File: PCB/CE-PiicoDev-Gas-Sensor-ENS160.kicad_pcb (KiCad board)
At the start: 2 copper layers, 25.4 x 25.4 mm, 34 parts, among them J1 , J2 , J3 Conn_01x05_Male, U1 ENS160, U2 Regulator 1V8

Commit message: v00
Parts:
- moved U2 4.13 mm to (93.6, 105.2), turned to 180 degrees
- moved R4 0.71 mm to (103.5, 106.6)
- moved C1 0.13 mm to (97.8, 98.8)
- renumbered ASW to ASW1
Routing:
- net +3V3: track 74.9 -> 79.8 mm
- net Net-(ASW1-Pad1): track 22.0 -> 24.4 mm, vias 0 -> 2
- net GND: track 10.2 -> 11.5 mm, vias 6 -> 8
- net /SCL: track 52.6 -> 53.8 mm

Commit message: Update CE-PiicoDev-Gas-Sensor-ENS160.kicad_pcb
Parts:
- removed kibuzzard-6271D9EE (x2): G***, kibuzzard-6271D9EE
- removed kibuzzard-6271DA35 (x2): G***, kibuzzard-6271DA35
- removed kibuzzard-6271DA5A (x2): G***, kibuzzard-6271DA5A
- removed kibuzzard-6271DA98 (x2): G***, kibuzzard-6271DA98
- removed kibuzzard-6271DAC1 (x2): G***, kibuzzard-6271DAC1
- added kibuzzard-62749DE2: G***, kibuzzard-62749DE2, B.Cu at (94.7, 110.1)
- added kibuzzard-62749DFD: G***, kibuzzard-62749DFD, F.Cu at (97.3, 110.0)
- added kibuzzard-62749DFD: G***, kibuzzard-62749DFD, B.Cu at (97.3, 110.0)
- added kibuzzard-62749E20: G***, kibuzzard-62749E20, F.Cu at (102.4, 110.4)
- added kibuzzard-62749E20: G***, kibuzzard-62749E20, B.Cu at (102.4, 110.4)
- added kibuzzard-62749E58: G***, kibuzzard-62749E58, F.Cu at (92.2, 110.1)
- added kibuzzard-62749E58: G***, kibuzzard-62749E58, B.Cu at (92.2, 110.1)
- added kibuzzard-62749E78: G***, kibuzzard-62749E78, F.Cu at (99.8, 109.9)
- added kibuzzard-62749E78: G***, kibuzzard-62749E78, B.Cu at (99.8, 109.9)
- added kibuzzard-62749F0B: G***, kibuzzard-62749F0B, F.Cu at (94.7, 110.1)
- renumbered ASW1 to ASW
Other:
- board text added: "ASW"
- board text added: "Designed at Core Electronics by Peter Johnston"
- board text added: "Pin Label Settings: font=Roboto-Bold text=GND l-cap=[ r-cap=] align=Right height=1.1 width=4.6 pad-top=3 pad-left=16 pad-right=3 pad-bot=3"
- board text removed: "Designed at Core Electronics"
- board text removed: "Pin Label Settings: font=Roboto text=GND l-cap=[ r-cap=] align=Left height=1.1 width=4.6 pad-top=2.5 pad-left=16 pad-right=2.5 pad-bot=2.5"

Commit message: Update CE-PiicoDev-Gas-Sensor-ENS160.kicad_pcb
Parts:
- removed kibuzzard-62749DE2: G***, kibuzzard-62749DE2
- removed kibuzzard-62749DFD (x2): G***, kibuzzard-62749DFD
- removed kibuzzard-62749E20 (x2): G***, kibuzzard-62749E20
- removed kibuzzard-62749E58 (x2): G***, kibuzzard-62749E58
- removed kibuzzard-62749E78 (x2): G***, kibuzzard-62749E78
- removed kibuzzard-62749F0B: G***, kibuzzard-62749F0B
- added kibuzzard-6285E559: G***, kibuzzard-6285E559, F.Cu at (94.7, 110.1)
- added kibuzzard-6285E559: G***, kibuzzard-6285E559, B.Cu at (94.7, 110.1)
- added kibuzzard-6285E568: G***, kibuzzard-6285E568, F.Cu at (97.3, 109.9)
- added kibuzzard-6285E568: G***, kibuzzard-6285E568, B.Cu at (97.3, 109.9)
- added kibuzzard-6285E695 (x2): G***, kibuzzard-6285E695, F.Cu at (92.2, 110.1)
- added kibuzzard-6285E695: G***, kibuzzard-6285E695, B.Cu at (92.2, 110.1)
- added kibuzzard-6285E748: G***, kibuzzard-6285E748, F.Cu at (99.8, 109.9)
- added kibuzzard-6285E748: G***, kibuzzard-6285E748, B.Cu at (99.8, 109.9)
- added kibuzzard-6285E79D: G***, kibuzzard-6285E79D, F.Cu at (102.4, 110.0)
- added kibuzzard-6285E79D: G***, kibuzzard-6285E79D, B.Cu at (102.4, 110.0)

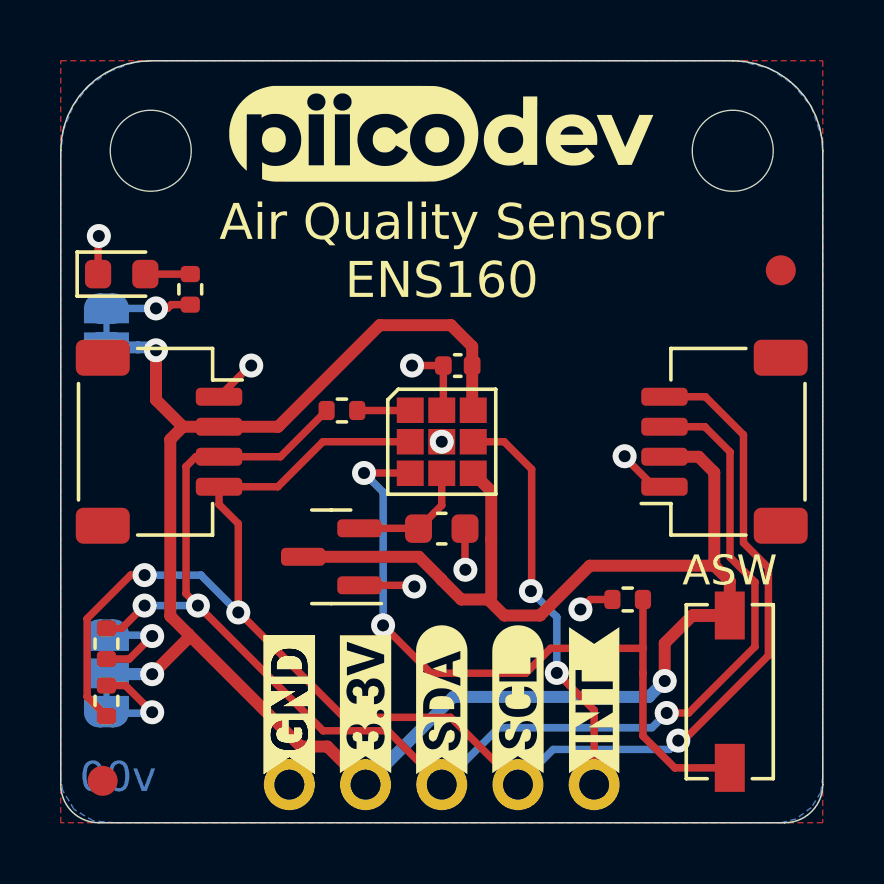
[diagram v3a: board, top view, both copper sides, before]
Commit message: Change default I2C address
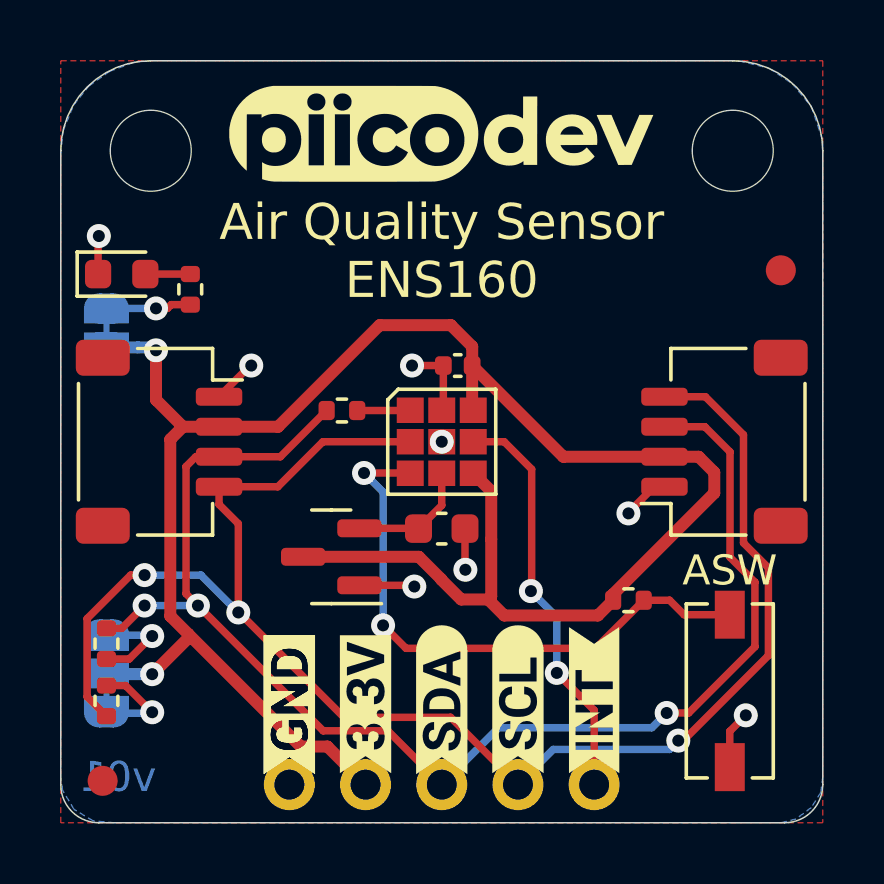
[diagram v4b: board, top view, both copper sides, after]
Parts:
- removed ASW: SW_DIP_x01, CoreElectronics_Components:SW_DIP_x01_Slide_CHS-01A1
- added ASW1: SW_DIP_x01, CoreElectronics_Components:SW_DIP_x01_Slide_CHS-01A1, F.Cu at (106.9, 109.7)
- moved LOGO1 1.25 mm to (106.9, 108.7)
- turned R4 to 0 degrees
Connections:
- R4 pad 1: Net-(ASW1-Pad1) -> +3V3
- R4 pad 2: GND -> Net-(U1-Pad3)
- U1 pad 3: Net-(ASW1-Pad1) -> Net-(U1-Pad3)
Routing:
- net Net-(ASW1-Pad1): track 24.4 -> 0.00 mm, vias 2 -> 0
- net Net-(U1-Pad3): track 0.00 -> 19.6 mm, vias 0 -> 2
- net +3V3: track 79.8 -> 67.8 mm, vias 3 -> 2
- net GND: track 11.5 -> 12.1 mm
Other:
- board text added: "ASW OFF 0x53 ASW ON 0x52"
- board text added: "v01"
- board text removed: "ASW OFF 0x52 ASW ON 0x53"
- board text removed: "v00"

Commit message: v10 release
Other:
- board text added: "v10"
- board text removed: "v01"
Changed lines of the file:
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@@
   (gr_line (start 84.582 112.776) (end 84.582 91.646) (layer "Edge.Cuts") (width 0.05))
   (gr_arc (start 84.582 91.646) (mid 85.46068 89.52468) (end 87.582 88.646) (layer "Edge.Cuts") (width 0.05))
-  (gr_text "v01" (at 86.492 112.522) (layer "B.Cu")
+  (gr_text "v10" (at 86.492 112.522) (layer "B.Cu")
     (effects (font (size 1 1) (thickness 0.2)) (justify mirror))
   )
